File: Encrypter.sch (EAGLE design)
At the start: 5 parts, among them IC1 PIC16LF1517/19P

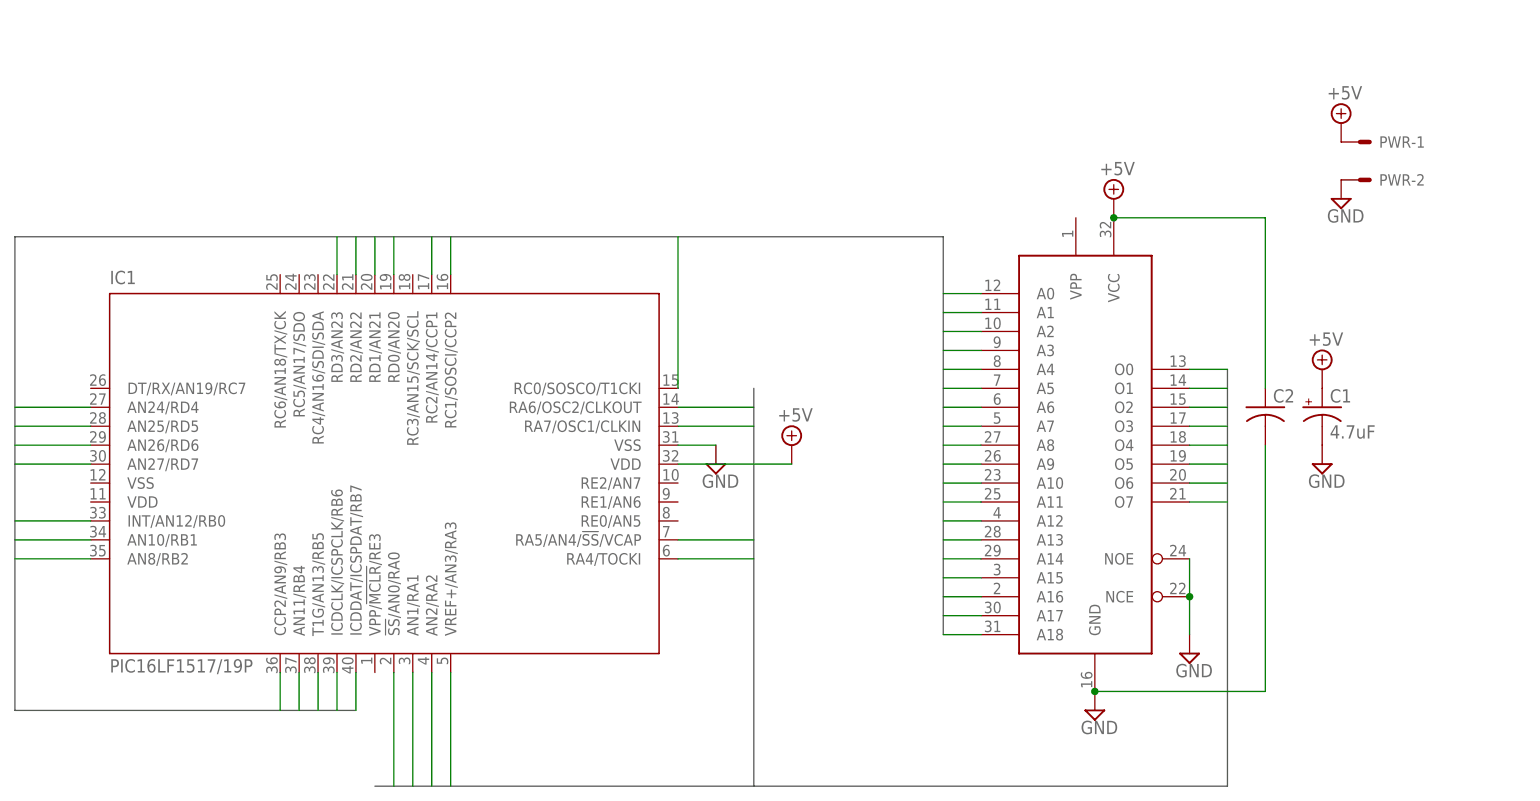
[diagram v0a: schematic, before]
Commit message: Encrypter work
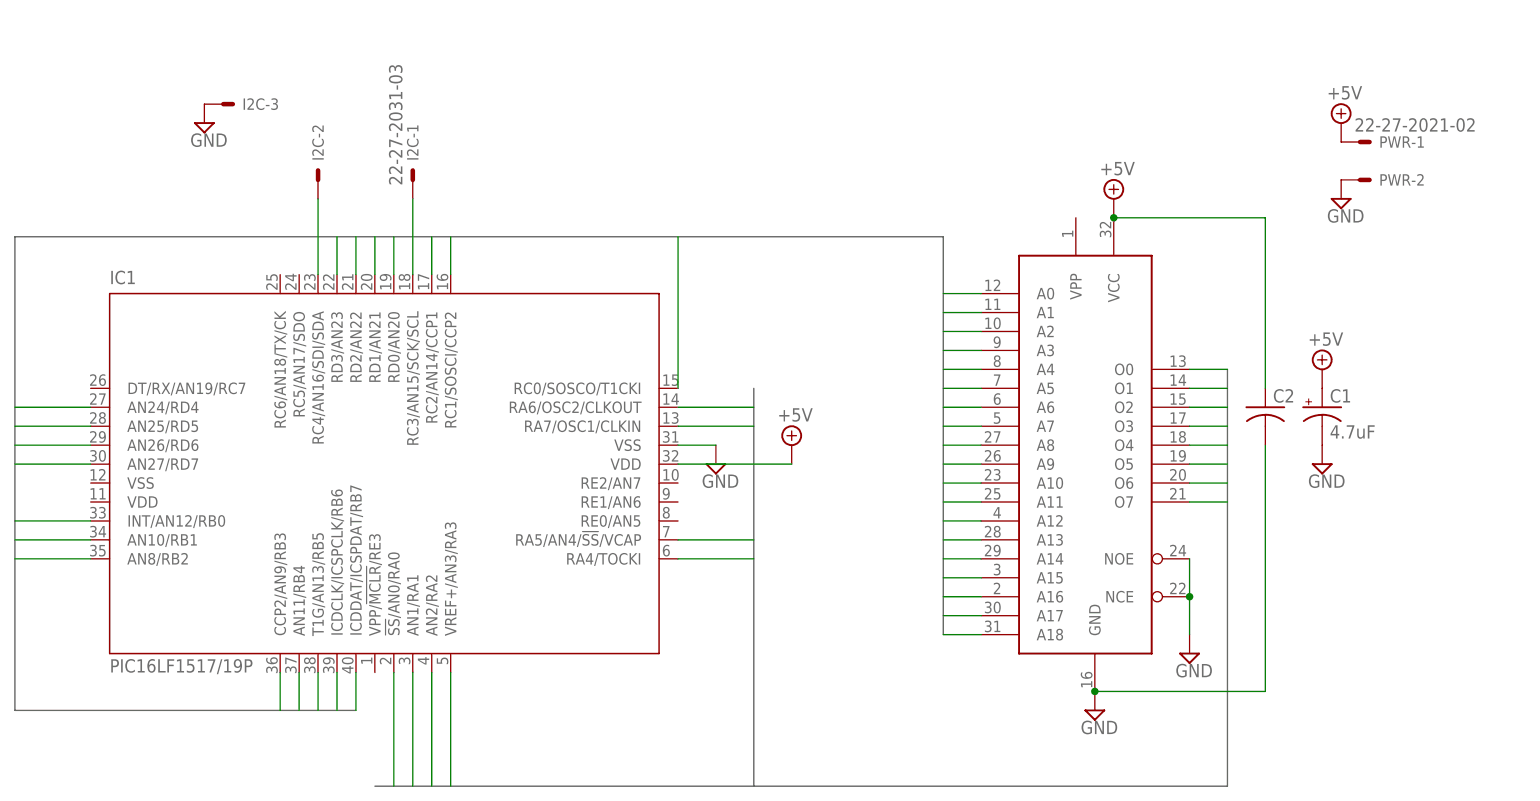
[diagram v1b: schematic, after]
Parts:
- added I2C: 22-27-2031-03, con-molex:22-27-2031-03
- PWR: value (none) -> 22-27-2021-02; device con-molex:KK-156-2 -> con-molex:22-27-2021-02
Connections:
- new net N$1: I2C-1.S, IC1.RC3/AN15/SCK/SCL
- new net N$2: I2C-2.S, IC1.RC4/AN16/SDI/SDA
- net GND: now also I2C-3.S
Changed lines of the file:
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@@
 <?xml version="1.0" encoding="utf-8"?>
 <!DOCTYPE eagle SYSTEM "eagle.dtd">
-<eagle version="7.6.0">
+<eagle version="7.2.0">
 <drawing>
 <settings>
@@
 <part name="SUPPLY7" library="supply2" deviceset="+5V" device=""/>
 <part name="C2" library="resistor" deviceset="C-US" device="050-025X075"/>
-<part name="PWR" library="con-molex" deviceset="KK-156-2" device=""/>
+<part name="PWR" library="con-molex" deviceset="22-?-02" device="27-2021"/>
 <part name="SUPPLY8" library="supply2" deviceset="+5V" device=""/>
 <part name="SUPPLY9" library="supply2" deviceset="GND" device=""/>
+<part name="I2C" library="con-molex" deviceset="22-?-03" device="27-2031"/>
+<part name="SUPPLY10" library="supply2" deviceset="GND" device=""/>
 </parts>
 <sheets>
@@
 <instance part="SUPPLY8" gate="+5V" x="35.56" y="83.82"/>
 <instance part="SUPPLY9" gate="GND" x="35.56" y="73.66"/>
+<instance part="I2C" gate="-1" x="-88.9" y="76.2" rot="R90"/>
+<instance part="I2C" gate="-2" x="-101.6" y="76.2" rot="R90"/>
+<instance part="I2C" gate="-3" x="-114.3" y="86.36"/>
+<instance part="SUPPLY10" gate="GND" x="-116.84" y="83.82"/>
 </instances>
 <busses>
@@
 <pinref part="SUPPLY9" gate="GND" pin="GND"/>
 </segment>
+<segment>
+<pinref part="I2C" gate="-3" pin="S"/>
+<pinref part="SUPPLY10" gate="GND" pin="GND"/>
+</segment>
 </net>
 <net name="A0" class="0">
@@
 </segment>
 </net>
+<net name="N$1" class="0">
+<segment>
+<pinref part="IC1" gate="G$1" pin="RC3/AN15/SCK/SCL"/>
+<pinref part="I2C" gate="-1" pin="S"/>
+<wire x1="-88.9" y1="73.66" x2="-88.9" y2="63.5" width="0.1524" layer="91"/>
+</segment>
+</net>
+<net name="N$2" class="0">
+<segment>
+<pinref part="IC1" gate="G$1" pin="RC4/AN16/SDI/SDA"/>
+<pinref part="I2C" gate="-2" pin="S"/>
+<wire x1="-101.6" y1="73.66" x2="-101.6" y2="63.5" width="0.1524" layer="91"/>
+</segment>
+</net>
